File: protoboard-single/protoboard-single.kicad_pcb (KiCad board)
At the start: 2 copper layers, 38.1 x 27.9 mm, 16 parts, among them J1 MODULE_HEADER, J10 MODULE_HEADER, J11 MODULE_HEADER, J12 MODULE_HEADER, J13 MODULE_HEADER, J14 MODULE_HEADER, J15 MODULE_HEADER, J2 MODULE_HEADER, J3 MODULE_HEADER, J4 MODULE_HEADER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

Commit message: production-ready files?
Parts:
- SILK1: footprint parts:TESSEL-HEXAGON-LOGO -> parts:TESSEL-HEXAGON-LOGO-BACK; moved to B.Cu
- moved SILK1 4.51 mm to (144.1, 101.6), turned to 270 degrees
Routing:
- net Net-(J1-Pad2): track 124.6 -> 128.1 mm
- net Net-(J1-Pad1): track 66.9 -> 70.4 mm
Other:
- rule pad_to_mask_clearance: 0 -> 0.0762
- board text added: "TM-15-00"
- board text added: "diy-module"
- board text added: "tessel.io"

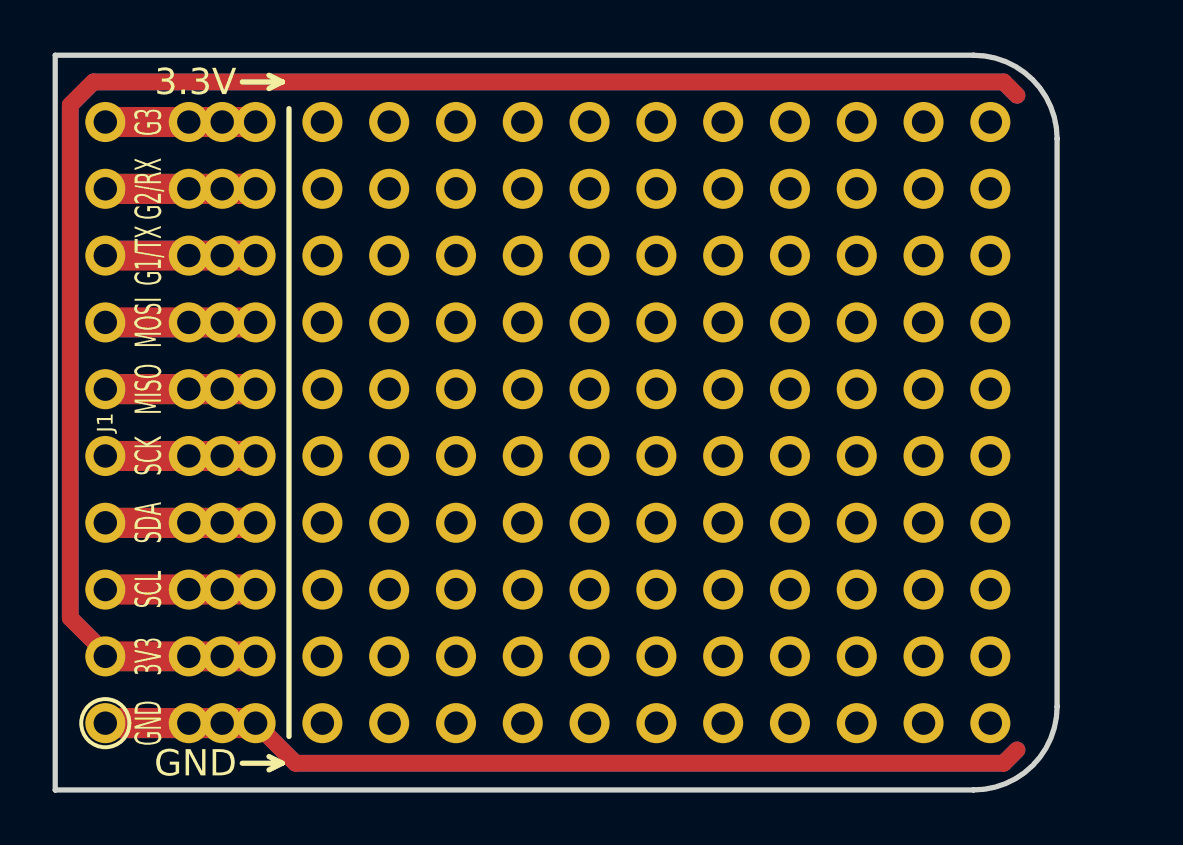
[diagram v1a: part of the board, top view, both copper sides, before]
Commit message: user feedback incorporated for single
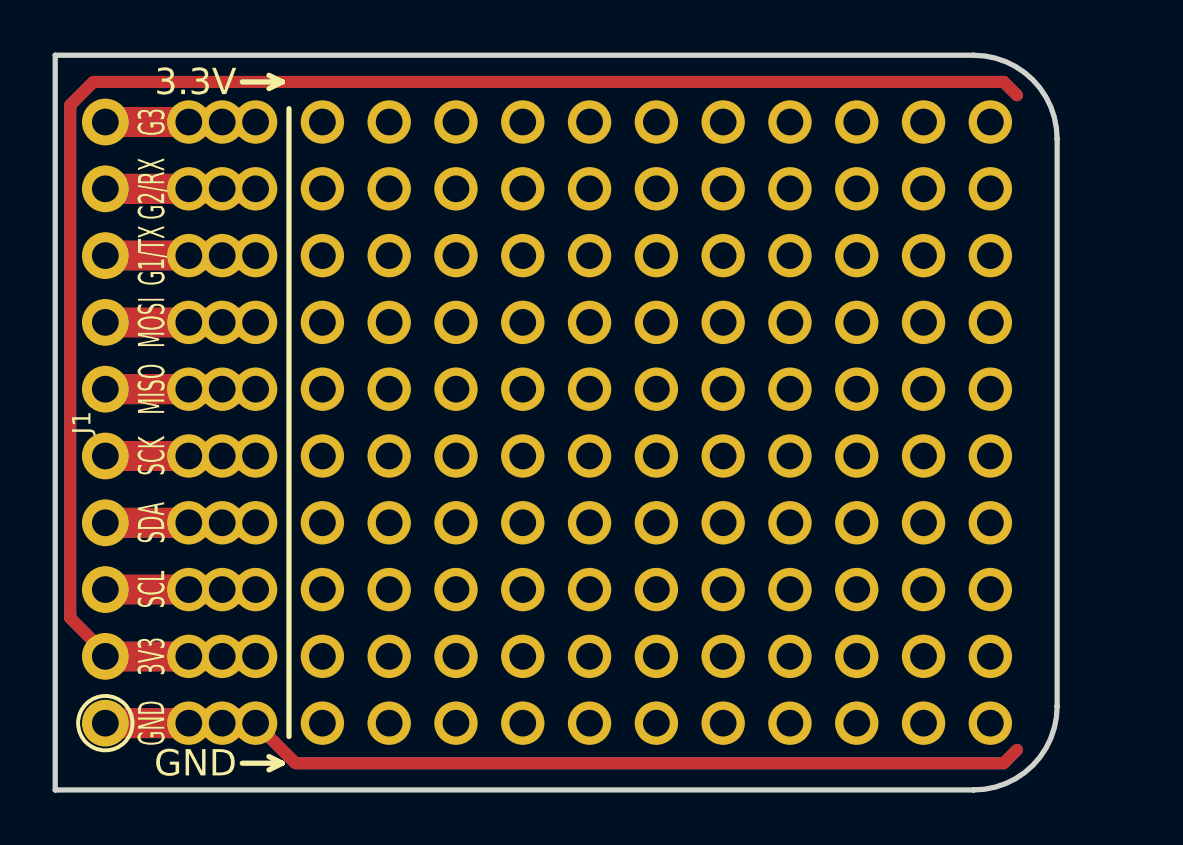
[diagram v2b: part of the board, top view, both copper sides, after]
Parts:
- J1: footprint parts:MODULE_HEADER_MODULE -> parts:MODULE_HEADER_MODULE_BIG
- J10, J11, J12, J13, J14, J15, J2, J3, J4, J5, J6, J7, J8, J9: footprint parts:1x10 -> parts:1x10_BIG
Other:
- net class Default: clearance 0.254 -> 0.2032
- rule trace_clearance: 0.254 -> 0.2032
